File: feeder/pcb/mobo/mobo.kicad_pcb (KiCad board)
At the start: 2 copper layers, 200 x 100 mm, 85 parts, among them J1 SWD_10, J2 FTDI_HEADER, J3 PLATED_PADS, M1 PEEL_MOTOR, M2 DRIVE_MOTOR, SW1 RESET, SW2 BUTTON_1, SW3 BUTTON_2, SW4 BOOT, U1 QRE1113, U2 STM32F103C8Tx, U3 TCS40DPR, U4 AP1117-33, U5 MCP16301, U6 DRV8833PWP, U7 MAX3078E, Y1 8MHz

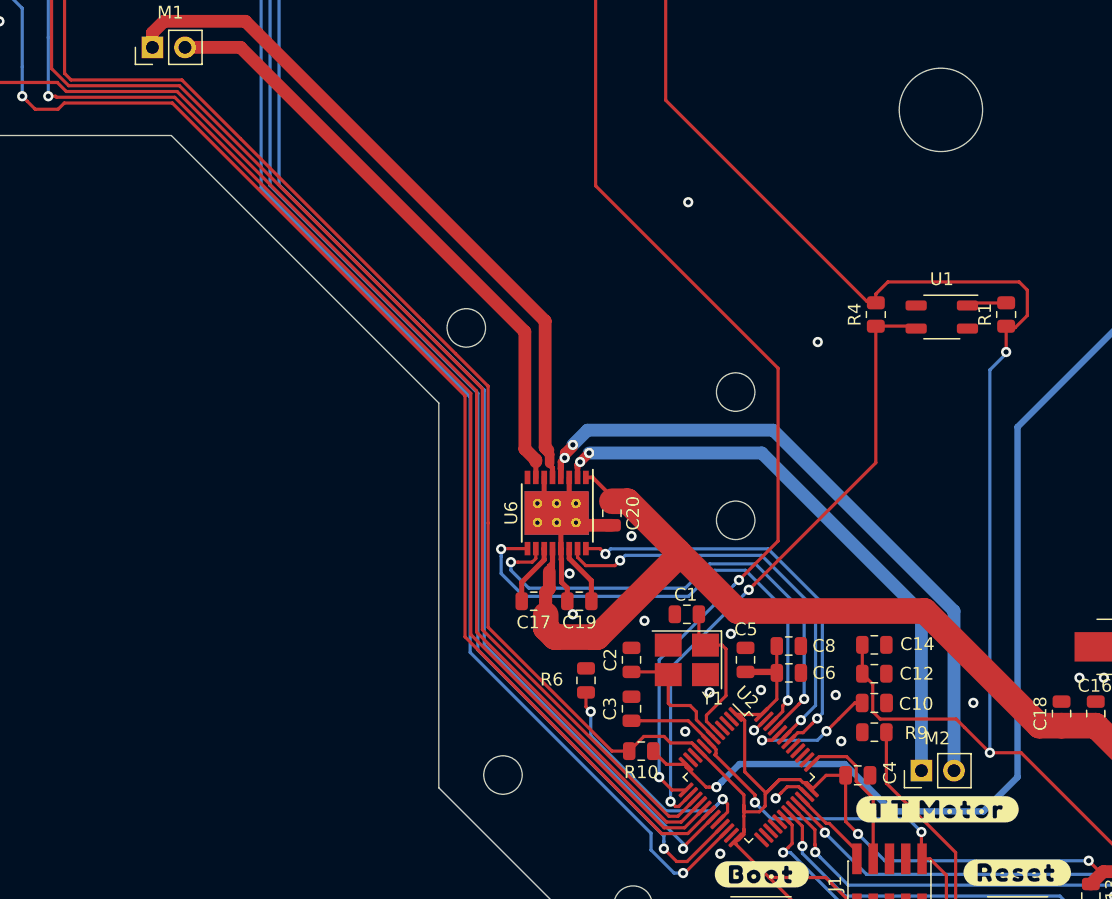
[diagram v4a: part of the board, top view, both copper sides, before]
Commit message: Changed labels
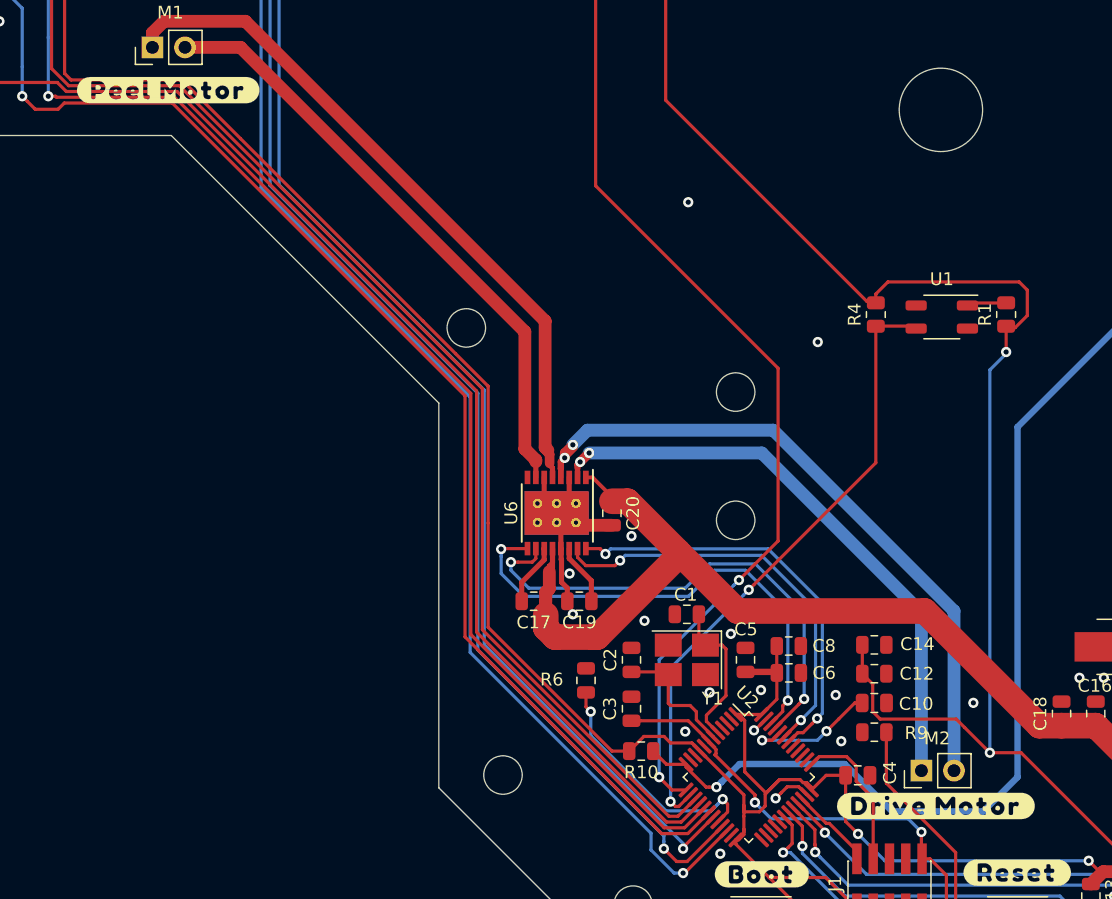
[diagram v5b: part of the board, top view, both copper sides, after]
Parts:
- removed the ? at (85.8, 92.9)
- added ?: , buzzard_labels, F.Cu at (85.7, 92.7)
- added ?: , buzzard_labels, F.Cu at (25.9, 36.9)
